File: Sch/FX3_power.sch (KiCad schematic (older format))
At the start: 19 parts, among them IC1 CYUSB3014

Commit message: modify
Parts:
- added C27: 0.01u, symbol C
- added C28: 0.1u, symbol C
- gave numbers to parts that had none: 18
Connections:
- net +2V5: now also IC1.B1 (VIO4), C27.1, C28.1
- net GND: now also C27.2, C28.2

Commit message: update
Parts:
- added C41, C42: 2.2u, symbol C
- added C43, C44, C46, C48, C49: 0.1u, symbol C
- added C45, C47: 0.01u, symbol C
- added L5, L6, L7, L8, L9: MPZ2012S601A, symbol L
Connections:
- net labels added: +3V3, +5V, CVDDQ, U3RXVDDQ, U3TXVDDQ, USB_VBUS, VBATT
- net labels removed: +2V5, FX3_VIO1, FX3_VIO5, VDDA
- wire segments 53 -> 76
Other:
- moved on the sheet: L1

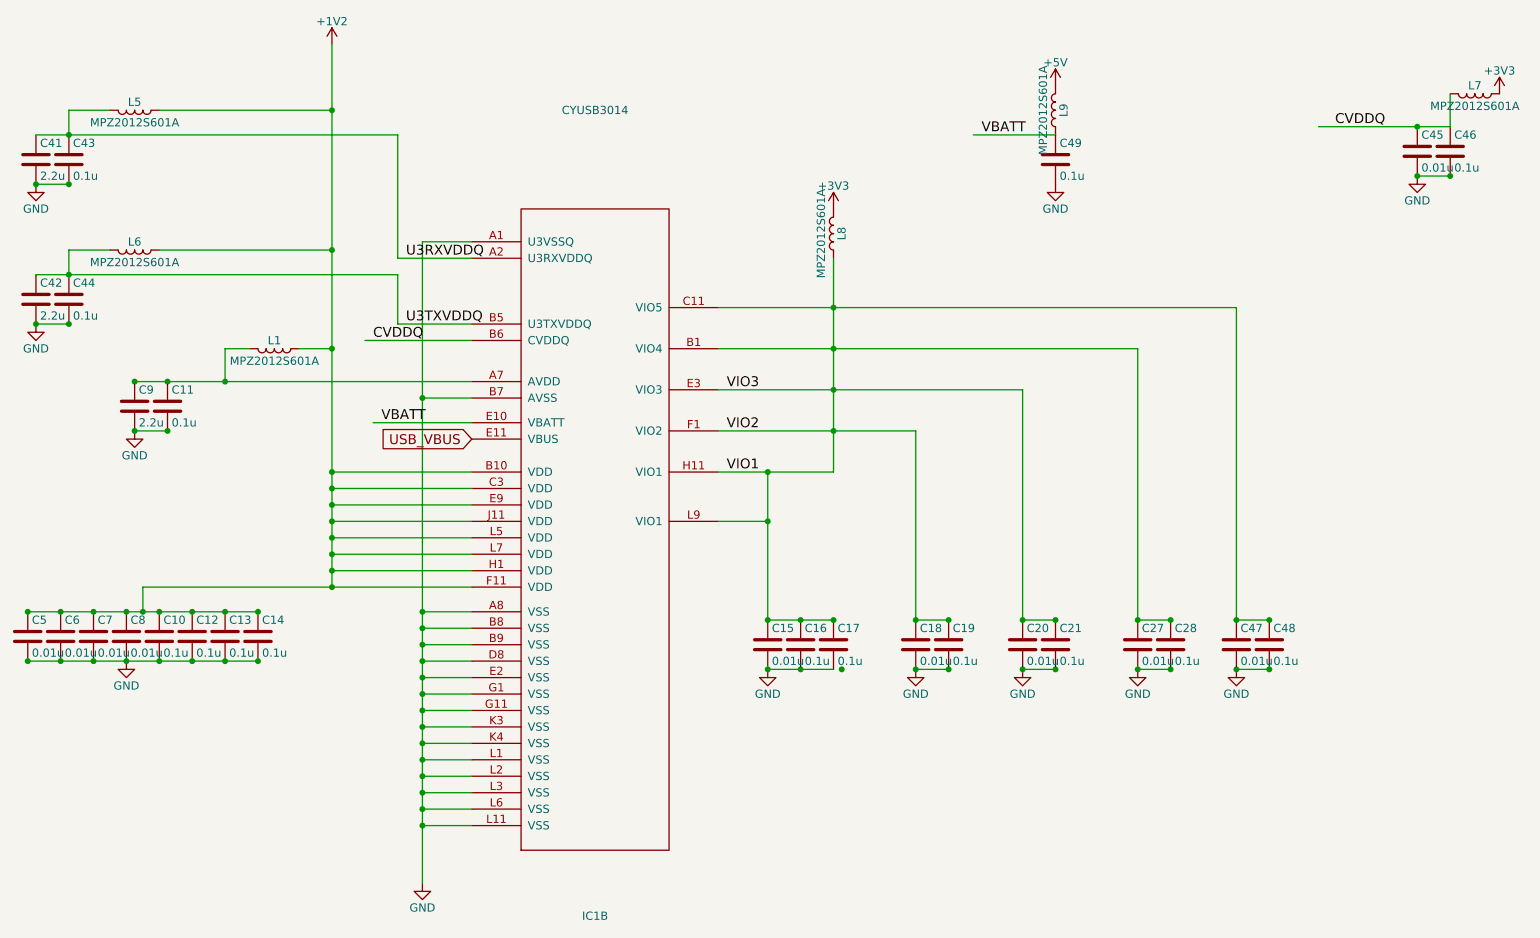
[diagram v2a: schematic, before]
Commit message: Add 1.2V
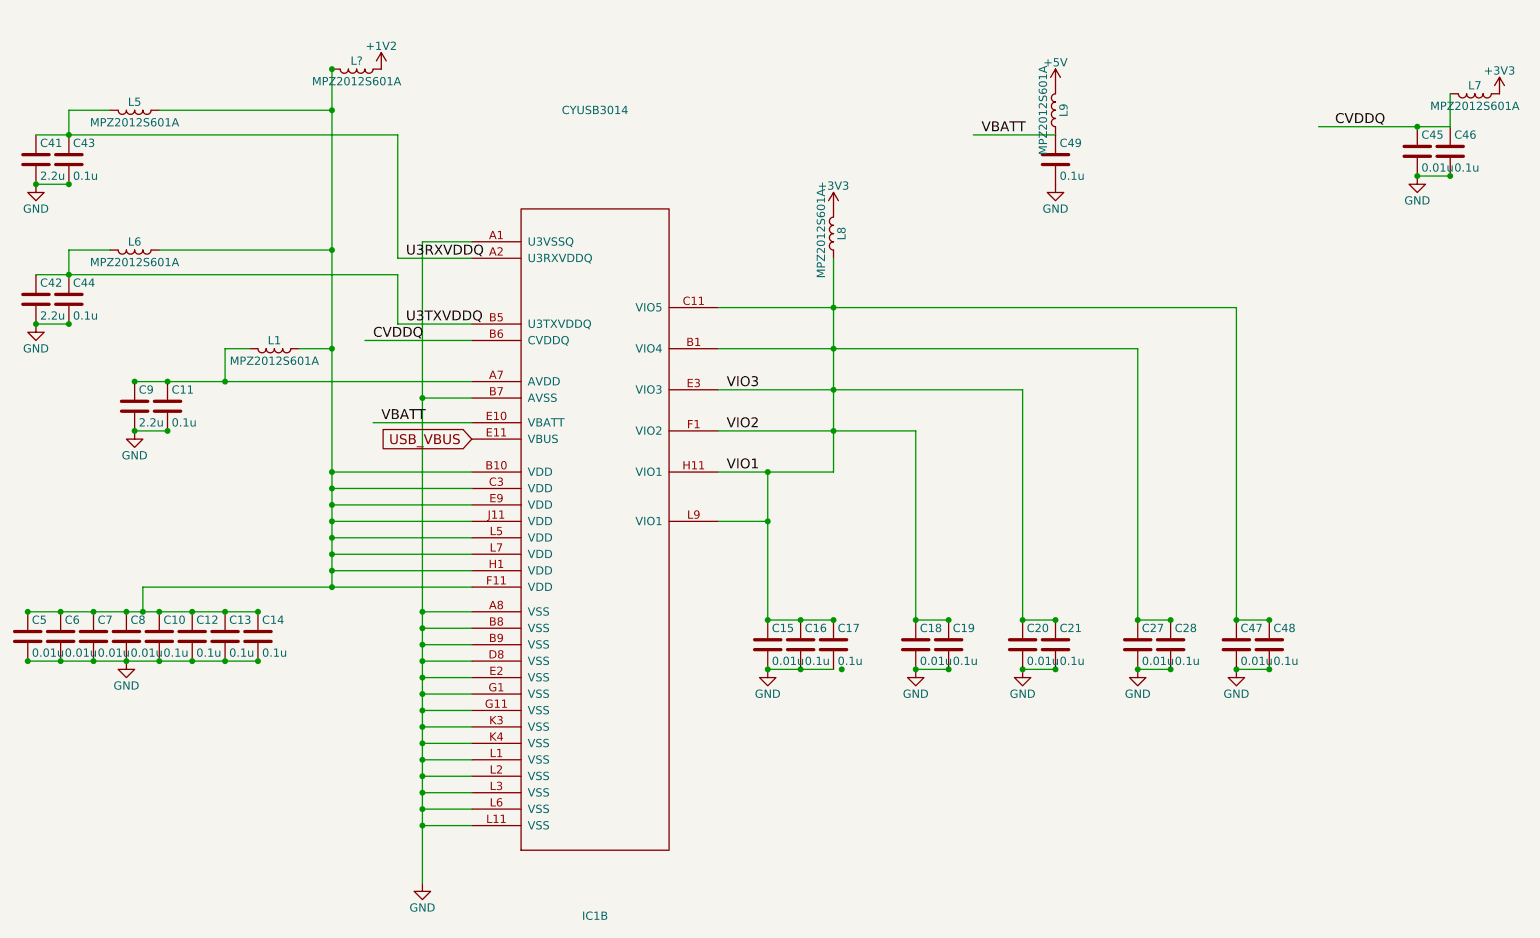
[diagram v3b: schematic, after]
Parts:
- added L?: MPZ2012S601A, symbol L
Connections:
- wire segments 76 -> 132
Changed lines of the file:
@@
 $Descr A4 11693 8268
 encoding utf-8
-Sheet 3 6
+Sheet 3 7
 Title ""
 Date ""
@@
 L +1V2 #PWR022
 U 1 1 58A09064
-P 3150 800
-F 0 "#PWR022" H 3150 650 50  0001 C CNN
-F 1 "+1V2" H 3150 940 50  0000 C CNN
-F 2 "" H 3150 800 50  0000 C CNN
-F 3 "" H 3150 800 50  0000 C CNN
-	1    3150 800
+P 3450 950
+F 0 "#PWR022" H 3450 800 50  0001 C CNN
+F 1 "+1V2" H 3450 1090 50  0000 C CNN
+F 2 "" H 3450 950 50  0000 C CNN
+F 3 "" H 3450 950 50  0000 C CNN
+	1    3450 950
 	1    0    0    -1
 $EndComp
@@
 $EndComp
 Wire Wire Line
-	5800 4600 6200 4600
+	5800 4600 6000 4600
+Wire Wire Line
+	6000 4600 6200 4600
 Connection ~ 6000 4600
 Wire Wire Line
-	5800 4300 6200 4300
+	5800 4300 6000 4300
+Wire Wire Line
+	6000 4300 6200 4300
 Connection ~ 6000 4300
 Wire Wire Line
-	6200 3400 5500 3400
-Wire Wire Line
-	5800 3400 5800 4300
+	6200 3400 5800 3400
+Wire Wire Line
+	5800 3400 5500 3400
+Wire Wire Line
+	5800 3400 5800 3700
+Wire Wire Line
+	5800 3700 5800 4300
 Wire Wire Line
 	5500 3700 5800 3700
@@
 Connection ~ 5800 3400
 Wire Wire Line
-	5500 3150 6700 3150
+	5500 3150 6200 3150
+Wire Wire Line
+	6200 3150 6700 3150
 Connection ~ 6200 3150
 Wire Wire Line
@@
 	3700 4750 4000 4750
 Wire Wire Line
-	3700 2000 3700 5900
+	3700 2000 3700 2950
+Wire Wire Line
+	3700 2950 3700 4250
+Wire Wire Line
+	3700 4250 3700 4350
+Wire Wire Line
+	3700 4350 3700 4450
+Wire Wire Line
+	3700 4450 3700 4550
+Wire Wire Line
+	3700 4550 3700 4650
+Wire Wire Line
+	3700 4650 3700 4750
+Wire Wire Line
+	3700 4750 3700 4850
+Wire Wire Line
+	3700 4850 3700 4950
+Wire Wire Line
+	3700 4950 3700 5050
+Wire Wire Line
+	3700 5050 3700 5150
+Wire Wire Line
+	3700 5150 3700 5250
+Wire Wire Line
+	3700 5250 3700 5350
+Wire Wire Line
+	3700 5350 3700 5450
+Wire Wire Line
+	3700 5450 3700 5550
+Wire Wire Line
+	3700 5550 3700 5900
 Wire Wire Line
 	4000 5150 3700 5150
@@
 	3150 4000 4000 4000
 Wire Wire Line
-	3150 800  3150 4100
-Wire Wire Line
 	4000 3500 3150 3500
 Connection ~ 3150 3500
@@
 Connection ~ 3150 3600
 Wire Wire Line
-	2000 4100 4000 4100
+	2000 4100 3150 4100
+Wire Wire Line
+	3150 4100 4000 4100
 Connection ~ 3150 4000
 Wire Wire Line
@@
 Connection ~ 3150 3400
 Wire Wire Line
-	1300 4550 2700 4550
+	1300 4550 1500 4550
+Wire Wire Line
+	1500 4550 1700 4550
+Wire Wire Line
+	1700 4550 1900 4550
+Wire Wire Line
+	1900 4550 2100 4550
+Wire Wire Line
+	2100 4550 2300 4550
+Wire Wire Line
+	2300 4550 2500 4550
+Wire Wire Line
+	2500 4550 2700 4550
 Connection ~ 2100 4550
 Wire Wire Line
-	1300 4250 2700 4250
+	1300 4250 1500 4250
+Wire Wire Line
+	1500 4250 1700 4250
+Wire Wire Line
+	1700 4250 1900 4250
+Wire Wire Line
+	1900 4250 2000 4250
+Wire Wire Line
+	2000 4250 2100 4250
+Wire Wire Line
+	2100 4250 2300 4250
+Wire Wire Line
+	2300 4250 2500 4250
+Wire Wire Line
+	2500 4250 2700 4250
 Connection ~ 1900 4550
 Connection ~ 2300 4550
@@
 	2500 2650 2650 2650
 Wire Wire Line
-	1950 2850 4000 2850
+	1950 2850 2150 2850
+Wire Wire Line
+	2150 2850 2500 2850
+Wire Wire Line
+	2500 2850 4000 2850
 Connection ~ 2500 2850
 Connection ~ 2150 2850
@@
 Connection ~ 1950 3150
 Wire Wire Line
-	5500 2650 8050 2650
+	5500 2650 6200 2650
+Wire Wire Line
+	6200 2650 8050 2650
 Connection ~ 6200 2650
 $Comp
@@
 	1550 2050 1550 2200
 Wire Wire Line
-	1350 2200 3550 2200
+	1350 2200 1550 2200
+Wire Wire Line
+	1550 2200 3550 2200
 $Comp
 L L L5
@@
 	1550 1200 1550 1350
 Wire Wire Line
-	1350 1350 3550 1350
+	1350 1350 1550 1350
+Wire Wire Line
+	1550 1350 3550 1350
 Connection ~ 3150 1200
 Wire Wire Line
@@
 Connection ~ 9750 1600
 Wire Wire Line
-	9150 1300 9950 1300
+	9150 1300 9750 1300
+Wire Wire Line
+	9750 1300 9950 1300
 $Comp
 L L L7
@@
 Connection ~ 8650 4600
 Wire Wire Line
-	5500 2400 8650 2400
+	5500 2400 6200 2400
+Wire Wire Line
+	6200 2400 8650 2400
 Wire Wire Line
 	2500 2850 2500 2650
 Connection ~ 3150 2650
 Wire Wire Line
-	6200 2100 6200 3400
+	6200 2100 6200 2400
+Wire Wire Line
+	6200 2400 6200 2650
+Wire Wire Line
+	6200 2650 6200 2900
+Wire Wire Line
+	6200 2900 6200 3150
+Wire Wire Line
+	6200 3150 6200 3400
 Connection ~ 6200 2400
 $Comp
@@
 $EndComp
 Wire Wire Line
-	5500 2900 7350 2900
+	5500 2900 6200 2900
+Wire Wire Line
+	6200 2900 7350 2900
 $Comp
 L +5V #PWR032
@@
 Text GLabel 4000 3200 0    60   Input ~ 0
 USB_VBUS
+$Comp
+L L L?
+U 1 1 58A55495
+P 3300 950
+F 0 "L?" V 3250 950 50  0000 C CNN
+F 1 "MPZ2012S601A" V 3375 950 50  0000 C CNN
+F 2 "" H 3300 950 50  0000 C CNN
+F 3 "" H 3300 950 50  0000 C CNN
+	1    3300 950
+	0    1    1    0
+$EndComp
+Wire Wire Line
+	3150 950  3150 1200
+Wire Wire Line
+	3150 1200 3150 2050
+Wire Wire Line
+	3150 2050 3150 2650
+Wire Wire Line
+	3150 2650 3150 3400
+Wire Wire Line
+	3150 3400 3150 3500
+Wire Wire Line
+	3150 3500 3150 3600
+Wire Wire Line
+	3150 3600 3150 3700
+Wire Wire Line
+	3150 3700 3150 3800
+Wire Wire Line
+	3150 3800 3150 3900
+Wire Wire Line
+	3150 3900 3150 4000
+Wire Wire Line
+	3150 4000 3150 4100
+Connection ~ 3150 950
 $EndSCHEMATC

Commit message: modify
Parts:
- gave numbers to parts that had none: 1
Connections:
- wire segments 132 -> 76
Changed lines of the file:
@@
 $EndComp
 Wire Wire Line
-	5800 4600 6000 4600
-Wire Wire Line
-	6000 4600 6200 4600
+	5800 4600 6200 4600
 Connection ~ 6000 4600
 Wire Wire Line
-	5800 4300 6000 4300
-Wire Wire Line
-	6000 4300 6200 4300
+	5800 4300 6200 4300
 Connection ~ 6000 4300
 Wire Wire Line
-	6200 3400 5800 3400
-Wire Wire Line
-	5800 3400 5500 3400
-Wire Wire Line
-	5800 3400 5800 3700
-Wire Wire Line
-	5800 3700 5800 4300
+	6200 3400 5500 3400
+Wire Wire Line
+	5800 3400 5800 4300
 Wire Wire Line
 	5500 3700 5800 3700
@@
 Connection ~ 5800 3400
 Wire Wire Line
-	5500 3150 6200 3150
-Wire Wire Line
-	6200 3150 6700 3150
+	5500 3150 6700 3150
 Connection ~ 6200 3150
 Wire Wire Line
@@
 	3700 4750 4000 4750
 Wire Wire Line
-	3700 2000 3700 2950
-Wire Wire Line
-	3700 2950 3700 4250
-Wire Wire Line
-	3700 4250 3700 4350
-Wire Wire Line
-	3700 4350 3700 4450
-Wire Wire Line
-	3700 4450 3700 4550
-Wire Wire Line
-	3700 4550 3700 4650
-Wire Wire Line
-	3700 4650 3700 4750
-Wire Wire Line
-	3700 4750 3700 4850
-Wire Wire Line
-	3700 4850 3700 4950
-Wire Wire Line
-	3700 4950 3700 5050
-Wire Wire Line
-	3700 5050 3700 5150
-Wire Wire Line
-	3700 5150 3700 5250
-Wire Wire Line
-	3700 5250 3700 5350
-Wire Wire Line
-	3700 5350 3700 5450
-Wire Wire Line
-	3700 5450 3700 5550
-Wire Wire Line
-	3700 5550 3700 5900
+	3700 2000 3700 5900
 Wire Wire Line
 	4000 5150 3700 5150
@@
 	3150 4000 4000 4000
 Wire Wire Line
-	4000 3500 3150 3500
+	3150 3500 4000 3500
 Connection ~ 3150 3500
 Wire Wire Line
-	4000 3900 3150 3900
+	3150 3900 4000 3900
 Connection ~ 3150 3900
 Wire Wire Line
-	4000 3600 3150 3600
+	3150 3600 4000 3600
 Connection ~ 3150 3600
 Wire Wire Line
-	2000 4100 3150 4100
-Wire Wire Line
-	3150 4100 4000 4100
+	2000 4100 4000 4100
 Connection ~ 3150 4000
 Wire Wire Line
-	4000 3800 3150 3800
+	3150 3800 4000 3800
 Connection ~ 3150 3800
 Wire Wire Line
-	4000 3700 3150 3700
+	3150 3700 4000 3700
 Connection ~ 3150 3700
 Wire Wire Line
-	4000 3400 3150 3400
+	3150 3400 4000 3400
 Connection ~ 3150 3400
 Wire Wire Line
-	1300 4550 1500 4550
-Wire Wire Line
-	1500 4550 1700 4550
-Wire Wire Line
-	1700 4550 1900 4550
-Wire Wire Line
-	1900 4550 2100 4550
-Wire Wire Line
-	2100 4550 2300 4550
-Wire Wire Line
-	2300 4550 2500 4550
-Wire Wire Line
-	2500 4550 2700 4550
+	1300 4550 2700 4550
 Connection ~ 2100 4550
 Wire Wire Line
-	1300 4250 1500 4250
-Wire Wire Line
-	1500 4250 1700 4250
-Wire Wire Line
-	1700 4250 1900 4250
-Wire Wire Line
-	1900 4250 2000 4250
-Wire Wire Line
-	2000 4250 2100 4250
-Wire Wire Line
-	2100 4250 2300 4250
-Wire Wire Line
-	2300 4250 2500 4250
-Wire Wire Line
-	2500 4250 2700 4250
+	1300 4250 2700 4250
 Connection ~ 1900 4550
 Connection ~ 2300 4550
@@
 Connection ~ 3150 4100
 Wire Wire Line
-	2950 2650 3150 2650
+	3150 2650 2950 2650
 Wire Wire Line
 	2500 2650 2650 2650
 Wire Wire Line
-	1950 2850 2150 2850
-Wire Wire Line
-	2150 2850 2500 2850
-Wire Wire Line
-	2500 2850 4000 2850
+	1950 2850 4000 2850
 Connection ~ 2500 2850
 Connection ~ 2150 2850
@@
 Connection ~ 1950 3150
 Wire Wire Line
-	5500 2650 6200 2650
-Wire Wire Line
-	6200 2650 8050 2650
+	5500 2650 8050 2650
 Connection ~ 6200 2650
 $Comp
@@
 $EndComp
 Wire Wire Line
-	2100 2050 3150 2050
+	3150 2050 2100 2050
 Connection ~ 3150 2050
 $Comp
@@
 	1550 2050 1550 2200
 Wire Wire Line
-	1350 2200 1550 2200
-Wire Wire Line
-	1550 2200 3550 2200
+	1350 2200 3550 2200
 $Comp
 L L L5
@@
 	1550 1200 1550 1350
 Wire Wire Line
-	1350 1350 1550 1350
-Wire Wire Line
-	1550 1350 3550 1350
+	1350 1350 3550 1350
 Connection ~ 3150 1200
 Wire Wire Line
@@
 Connection ~ 9750 1600
 Wire Wire Line
-	9150 1300 9750 1300
-Wire Wire Line
-	9750 1300 9950 1300
+	9150 1300 9950 1300
 $Comp
 L L L7
@@
 Connection ~ 8650 4600
 Wire Wire Line
-	5500 2400 6200 2400
-Wire Wire Line
-	6200 2400 8650 2400
+	5500 2400 8650 2400
 Wire Wire Line
 	2500 2850 2500 2650
 Connection ~ 3150 2650
 Wire Wire Line
-	6200 2100 6200 2400
-Wire Wire Line
-	6200 2400 6200 2650
-Wire Wire Line
-	6200 2650 6200 2900
-Wire Wire Line
-	6200 2900 6200 3150
-Wire Wire Line
-	6200 3150 6200 3400
+	6200 2100 6200 3400
 Connection ~ 6200 2400
 $Comp
@@
 $EndComp
 Wire Wire Line
-	5500 2900 6200 2900
-Wire Wire Line
-	6200 2900 7350 2900
+	5500 2900 7350 2900
 $Comp
 L +5V #PWR032
@@
 USB_VBUS
 $Comp
-L L L?
+L L L12
 U 1 1 58A55495
 P 3300 950
-F 0 "L?" V 3250 950 50  0000 C CNN
+F 0 "L12" V 3250 950 50  0000 C CNN
 F 1 "MPZ2012S601A" V 3375 950 50  0000 C CNN
 F 2 "" H 3300 950 50  0000 C CNN
@@
 $EndComp
 Wire Wire Line
-	3150 950  3150 1200
-Wire Wire Line
-	3150 1200 3150 2050
-Wire Wire Line
-	3150 2050 3150 2650
-Wire Wire Line
-	3150 2650 3150 3400
-Wire Wire Line
-	3150 3400 3150 3500
-Wire Wire Line
-	3150 3500 3150 3600
-Wire Wire Line
-	3150 3600 3150 3700
-Wire Wire Line
-	3150 3700 3150 3800
-Wire Wire Line
-	3150 3800 3150 3900
-Wire Wire Line
-	3150 3900 3150 4000
-Wire Wire Line
-	3150 4000 3150 4100
+	3150 950  3150 4100
 Connection ~ 3150 950
 $EndSCHEMATC
